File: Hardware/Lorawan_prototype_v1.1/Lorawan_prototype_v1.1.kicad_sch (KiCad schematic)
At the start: 130 parts, among them J7 THD2528-11SD-GF, U3 STM32F103RCTx

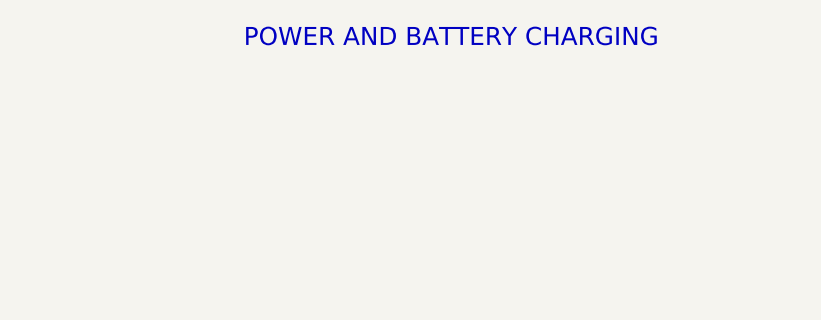
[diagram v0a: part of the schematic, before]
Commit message: optimized organization of components and routes, and added an i2c expansion pinout
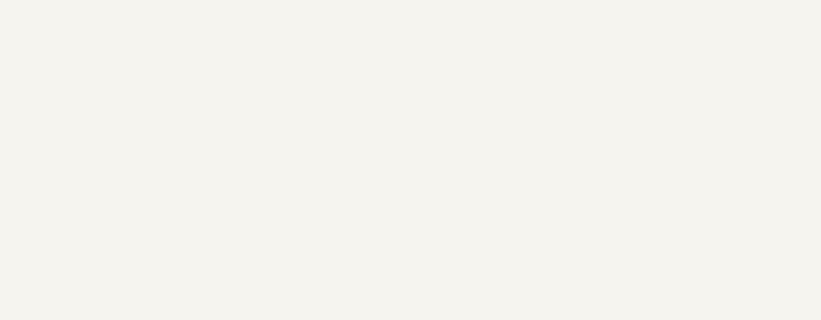
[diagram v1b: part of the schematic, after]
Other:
- note removed: "POWER AND BATTERY CHARGING"
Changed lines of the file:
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@@
     (effects (font (size 1.27 1.27)) (justify left bottom))
-  )
-  (text "POWER AND BATTERY CHARGING\n\n" (at 273.05 -19.05 0)
-    (effects (font (size 2 2)) (justify right bottom))
   )
   (text "12v inpout\n" (at 33.02 21.59 0)

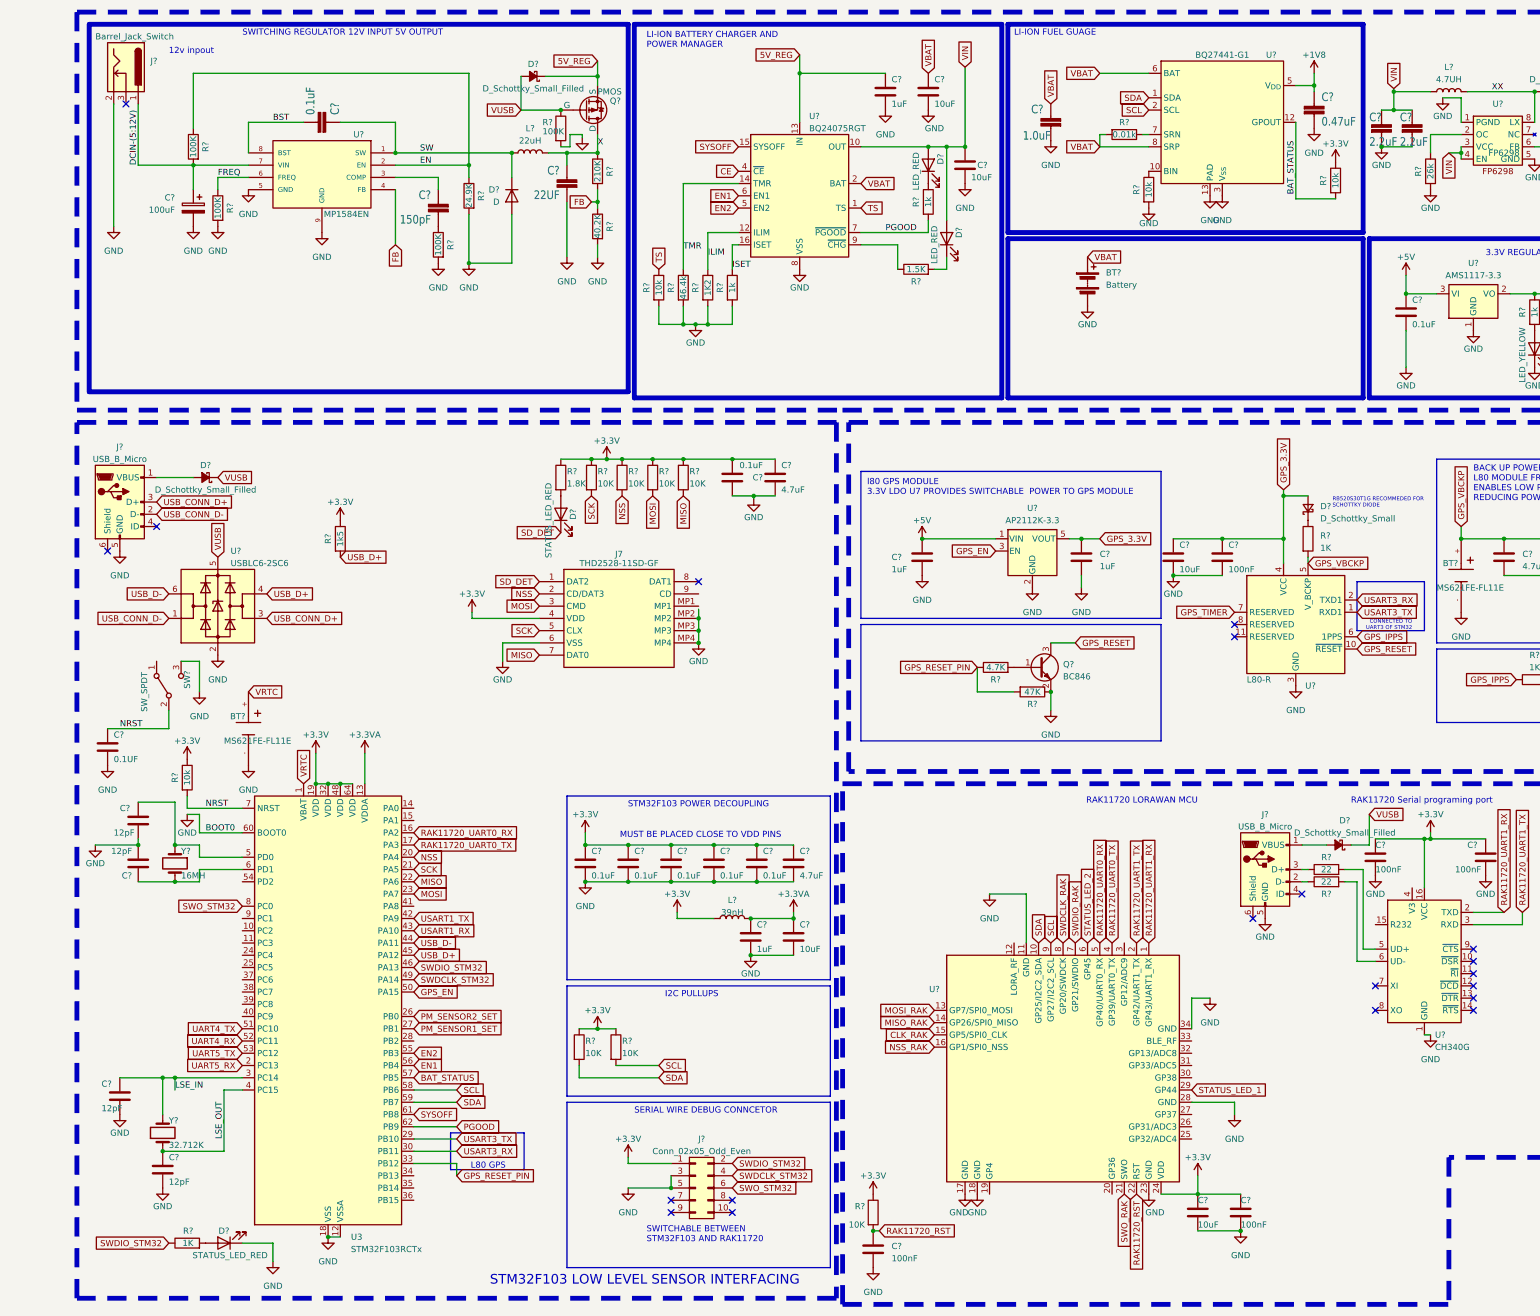
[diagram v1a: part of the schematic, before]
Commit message: optimized placement and routing of componenets
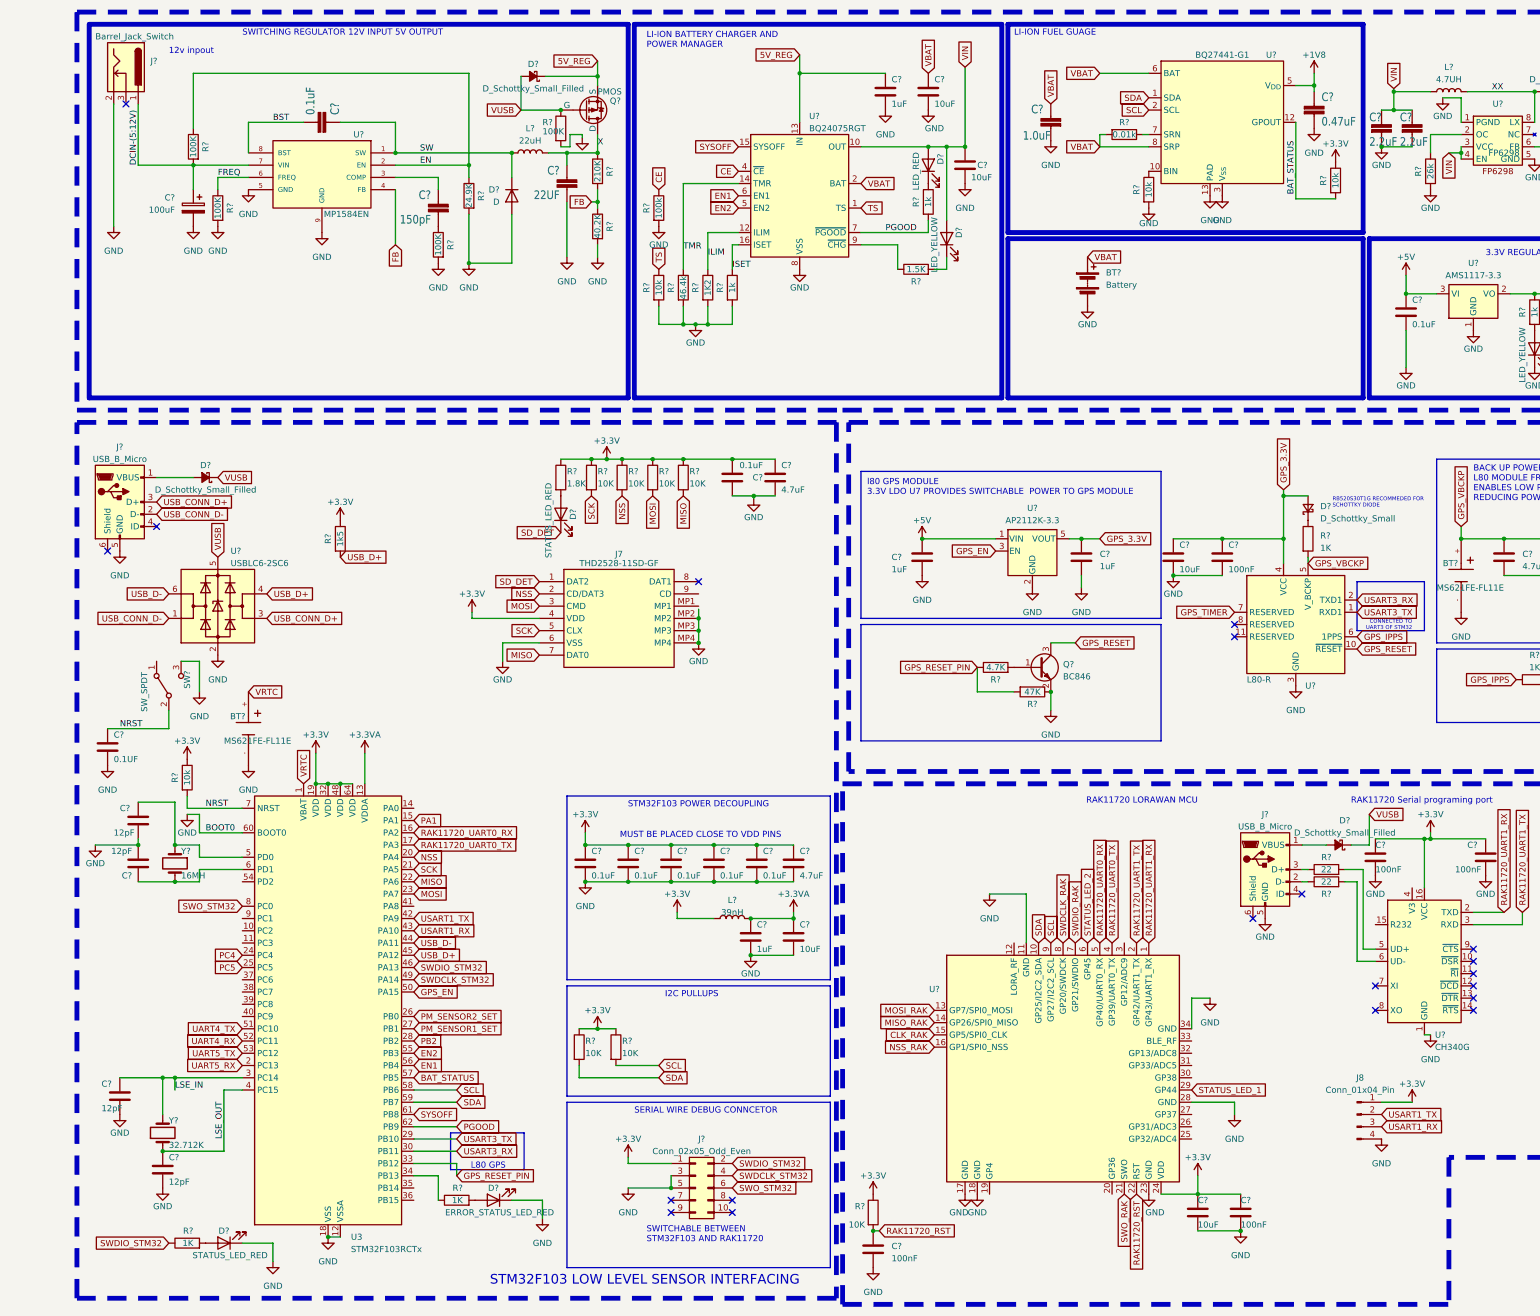
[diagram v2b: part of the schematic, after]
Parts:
- added D?: ERROR_STATUS_LED_RED, LED_SMD:LED_0603_1608Metric, symbol Device:LED
- added J8: Conn_01x04_Pin, Connector_PinHeader_2.54mm:PinHeader_1x04_P2.54mm_Vertical, symbol Connector:Conn_01x04_Pin
- added R?: 100k, Resistor_SMD:R_0603_1608Metric, symbol Device:R
- added R?: 1K, Resistor_SMD:R_0603_1608Metric, symbol Device:R
- D?: value LED_RED -> LED_YELLOW
- J7: footprint THD252811SDGF -> microSdcard:THD252811SDGF
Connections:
- net +3.3V: now also J8.1 (Pin_1)
- net CE: now also R?.1
- net GND: now also D?.1 (K), J8.4 (Pin_4), R?.2
- net USART1_RX: now also J8.3 (Pin_3)
- net USART1_TX: now also J8.2 (Pin_2)
- net PA1: now reaches U3.15 (PA1)
- net PC4: now reaches U3.24 (PC4)
- net PC5: now reaches U3.25 (PC5)
- net PB2: now reaches U3.28 (PB2)
- net at U3.34 (PB13): now also R?.1
- new net: D?.2 (A), R?.2
